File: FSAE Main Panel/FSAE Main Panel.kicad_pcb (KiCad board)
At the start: 2 copper layers, 1 part

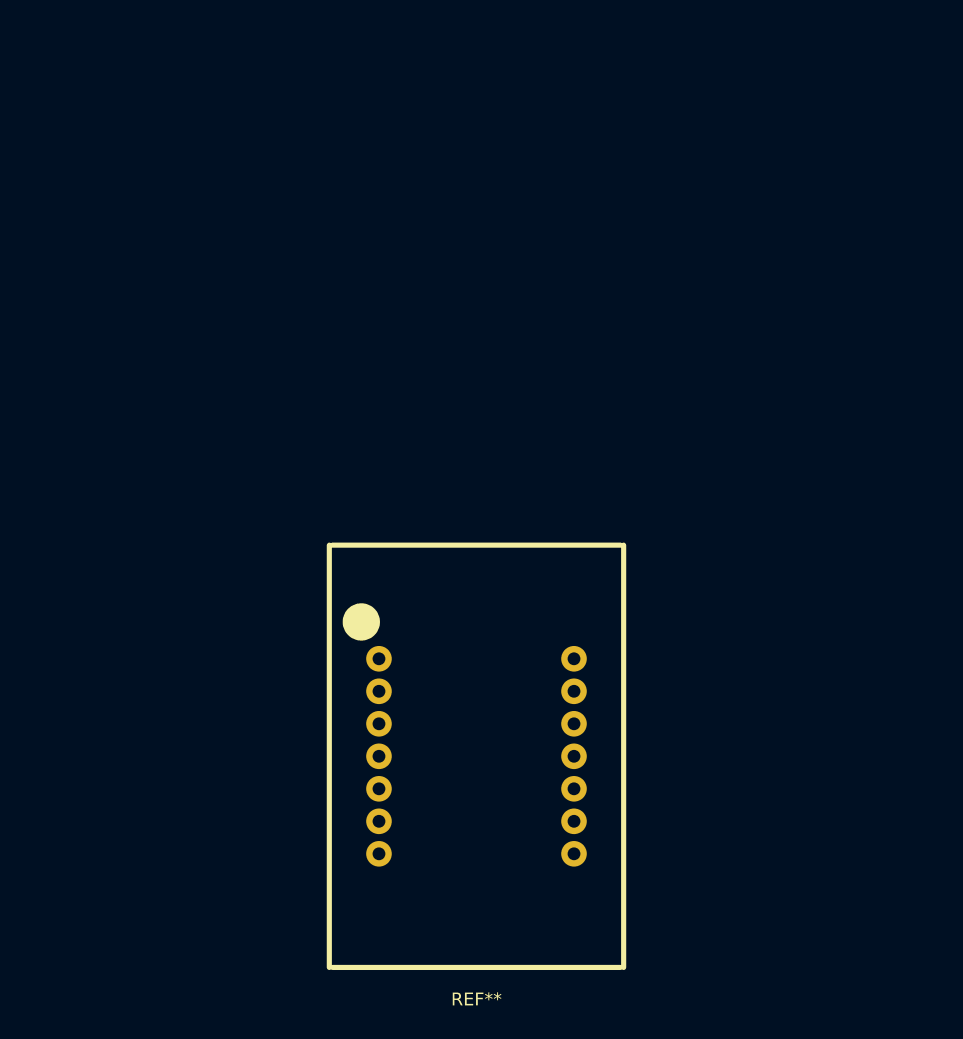
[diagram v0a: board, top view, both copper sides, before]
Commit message: Initial PCB layout
Started PCB layout with major dimensions.
Added RPM LEDs.
Rearranged the file structure for the librarys and the search paths.
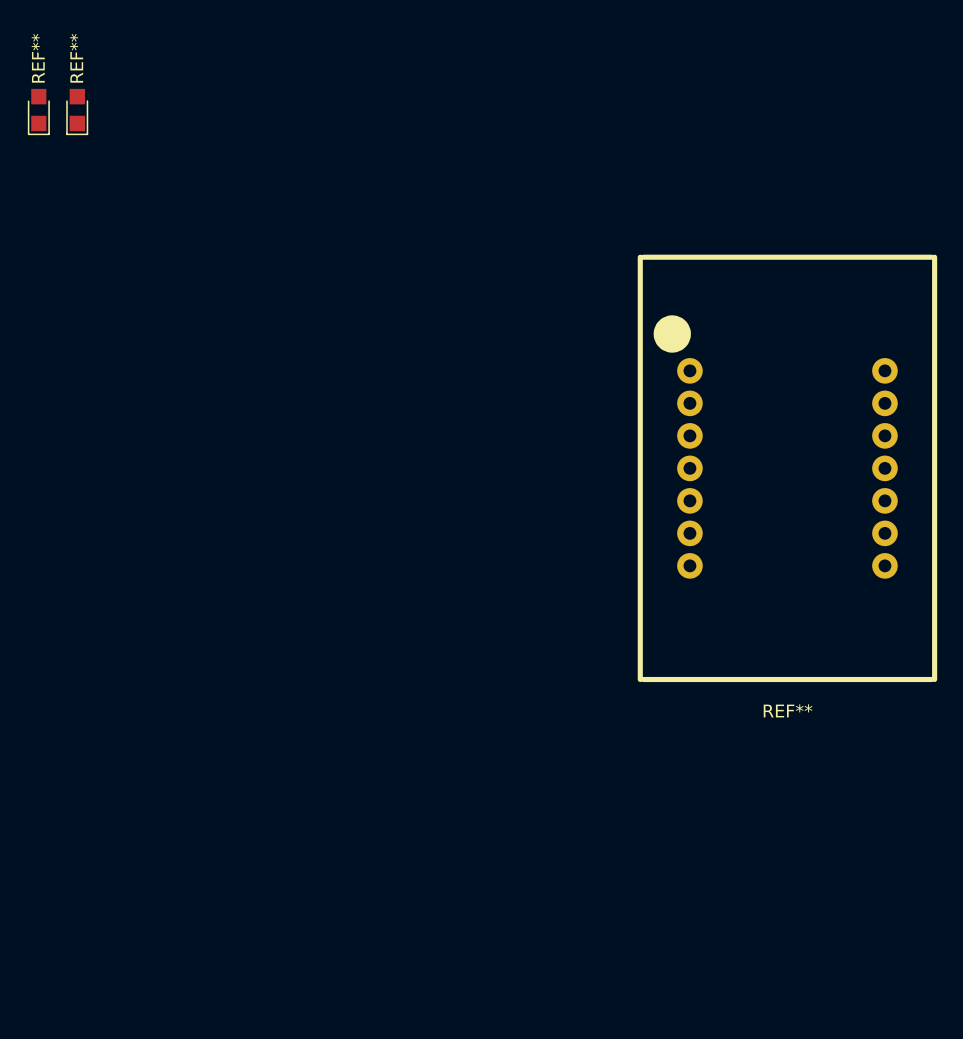
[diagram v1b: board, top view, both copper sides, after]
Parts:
- added REF**: LED_0805, OSRAM:D_0805, F.Cu at (104.0, 37.5)
- added REF**: LED_0805, OSRAM:D_0805, F.Cu at (107.0, 37.5)
- moved REF** 33.1 mm to (162.5, 65.5)
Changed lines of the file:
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@@
     (links 0)
     (no_connects 0)
-    (area 0 0 0 0)
+    (area 124.924999 69.724999 151.475001 108.075)
     (thickness 1.6)
-    (drawings 0)
+    (drawings 13)
     (tracks 0)
     (zones 0)
-    (modules 1)
+    (modules 3)
     (nets 1)
   )
@@
     (pad_to_mask_clearance 0.2)
     (aux_axis_origin 0 0)
-    (visible_elements FFFFFF7F)
+    (visible_elements 7FFFFFFF)
     (pcbplotparams
       (layerselection 0x00030_80000001)
@@
   )
   (module Kingbright:SC10-11EWA (layer F.Cu)
-    (at 138.2 88)
+    (at 162.5 65.5)
     (tags "26mm 7 segment")
     (fp_text reference REF** (at 0 19) (layer F.SilkS)
@@
     (pad 1 thru_hole circle (at -7.62 -7.62) (size 2 2) (drill 1) (layers *.Cu *.Mask))
   )
+  (module OSRAM:D_0805 (layer F.Cu)
+    (at 104 37.5 90)
+    (descr "Diode SMD in 0805 package http://datasheets.avx.com/schottky.pdf")
+    (tags "smd diode")
+    (attr smd)
+    (fp_text reference REF** (at 4 0 90) (layer F.SilkS)
+      (effects (font (size 1 1) (thickness 0.15)))
+    )
+    (fp_text value LED_0805 (at -6 0 90) (layer F.Fab)
+      (effects (font (size 1 1) (thickness 0.15)))
+    )
+    (fp_line (start -0.1 -0.4) (end -0.1 0.4) (layer F.Fab) (width 0.05))
+    (fp_text user %R (at 4 0 90) (layer F.Fab)
+      (effects (font (size 1 1) (thickness 0.15)))
+    )
+    (fp_line (start -1.9 -0.8) (end -1.9 0.8) (layer F.SilkS) (width 0.12))
+    (fp_line (start -2 0.88) (end -2 -0.88) (layer F.CrtYd) (width 0.05))
+    (fp_line (start 1.7 0.88) (end -2 0.88) (layer F.CrtYd) (width 0.05))
+    (fp_line (start 1.7 -0.88) (end 1.7 0.88) (layer F.CrtYd) (width 0.05))
+    (fp_line (start -2 -0.88) (end 1.7 -0.88) (layer F.CrtYd) (width 0.05))
+    (fp_line (start 0.2 0) (end 0.4 0) (layer F.Fab) (width 0.1))
+    (fp_line (start 0.2 0.2) (end 0.2 -0.2) (layer F.Fab) (width 0.1))
+    (fp_line (start -0.1 0) (end 0.2 0.2) (layer F.Fab) (width 0.1))
+    (fp_line (start 0.2 -0.2) (end -0.1 0) (layer F.Fab) (width 0.1))
+    (fp_line (start -1 0.65) (end -1 -0.65) (layer F.Fab) (width 0.1))
+    (fp_line (start 1 0.65) (end -1 0.65) (layer F.Fab) (width 0.1))
+    (fp_line (start 1 -0.65) (end 1 0.65) (layer F.Fab) (width 0.1))
+    (fp_line (start -1 -0.65) (end 1 -0.65) (layer F.Fab) (width 0.1))
+    (fp_line (start -1.9 0.8) (end 0.7 0.8) (layer F.SilkS) (width 0.12))
+    (fp_line (start -1.9 -0.8) (end 0.7 -0.8) (layer F.SilkS) (width 0.12))
+    (pad 1 smd rect (at -1.05 0 90) (size 1.2 1.2) (layers F.Cu F.Paste F.Mask))
+    (pad 2 smd rect (at 1.05 0 90) (size 1.2 1.2) (layers F.Cu F.Paste F.Mask))
+    (model ${KISYS3DMOD}/Diodes_SMD.3dshapes/D_0805.wrl
+      (at (xyz 0 0 0))
+      (scale (xyz 1 1 1))
+      (rotate (xyz 0 0 0))
+    )
+  )
+  (module OSRAM:D_0805 (layer F.Cu)
+    (at 107 37.5 90)
+    (descr "Diode SMD in 0805 package http://datasheets.avx.com/schottky.pdf")
+    (tags "smd diode")
+    (attr smd)
+    (fp_text reference REF** (at 4 0 90) (layer F.SilkS)
+      (effects (font (size 1 1) (thickness 0.15)))
+    )
+    (fp_text value LED_0805 (at -6 0 90) (layer F.Fab)
+      (effects (font (size 1 1) (thickness 0.15)))
+    )
+    (fp_line (start -0.1 -0.4) (end -0.1 0.4) (layer F.Fab) (width 0.05))
+    (fp_text user %R (at 4 0 90) (layer F.Fab)
+      (effects (font (size 1 1) (thickness 0.15)))
+    )
+    (fp_line (start -1.9 -0.8) (end -1.9 0.8) (layer F.SilkS) (width 0.12))
+    (fp_line (start -2 0.88) (end -2 -0.88) (layer F.CrtYd) (width 0.05))
+    (fp_line (start 1.7 0.88) (end -2 0.88) (layer F.CrtYd) (width 0.05))
+    (fp_line (start 1.7 -0.88) (end 1.7 0.88) (layer F.CrtYd) (width 0.05))
+    (fp_line (start -2 -0.88) (end 1.7 -0.88) (layer F.CrtYd) (width 0.05))
+    (fp_line (start 0.2 0) (end 0.4 0) (layer F.Fab) (width 0.1))
+    (fp_line (start 0.2 0.2) (end 0.2 -0.2) (layer F.Fab) (width 0.1))
+    (fp_line (start -0.1 0) (end 0.2 0.2) (layer F.Fab) (width 0.1))
+    (fp_line (start 0.2 -0.2) (end -0.1 0) (layer F.Fab) (width 0.1))
+    (fp_line (start -1 0.65) (end -1 -0.65) (layer F.Fab) (width 0.1))
+    (fp_line (start 1 0.65) (end -1 0.65) (layer F.Fab) (width 0.1))
+    (fp_line (start 1 -0.65) (end 1 0.65) (layer F.Fab) (width 0.1))
+    (fp_line (start -1 -0.65) (end 1 -0.65) (layer F.Fab) (width 0.1))
+    (fp_line (start -1.9 0.8) (end 0.7 0.8) (layer F.SilkS) (width 0.12))
+    (fp_line (start -1.9 -0.8) (end 0.7 -0.8) (layer F.SilkS) (width 0.12))
+    (pad 1 smd rect (at -1.05 0 90) (size 1.2 1.2) (layers F.Cu F.Paste F.Mask))
+    (pad 2 smd rect (at 1.05 0 90) (size 1.2 1.2) (layers F.Cu F.Paste F.Mask))
+    (model ${KISYS3DMOD}/Diodes_SMD.3dshapes/D_0805.wrl
+      (at (xyz 0 0 0))
+      (scale (xyz 1 1 1))
+      (rotate (xyz 0 0 0))
+    )
+  )
+  (dimension 8 (width 0.3) (layer Margin)
+    (gr_text 8mm (at 177.85 45 270) (layer Margin)
+      (effects (font (size 1.5 1.5) (thickness 0.3)))
+    )
+    (feature1 (pts (xy 174 49) (xy 179.2 49)))
+    (feature2 (pts (xy 174 41) (xy 179.2 41)))
+    (crossbar (pts (xy 176.5 41) (xy 176.5 49)))
+    (arrow1a (pts (xy 176.5 49) (xy 175.913579 47.873496)))
+    (arrow1b (pts (xy 176.5 49) (xy 177.086421 47.873496)))
+    (arrow2a (pts (xy 176.5 41) (xy 175.913579 42.126504)))
+    (arrow2b (pts (xy 176.5 41) (xy 177.086421 42.126504)))
+  )
+  (dimension 33 (width 0.3) (layer Margin)
+    (gr_text 33mm (at 177.85 65.5 270) (layer Margin)
+      (effects (font (size 1.5 1.5) (thickness 0.3)))
+    )
+    (feature1 (pts (xy 174 82) (xy 179.2 82)))
+    (feature2 (pts (xy 174 49) (xy 179.2 49)))
+    (crossbar (pts (xy 176.5 49) (xy 176.5 82)))
+    (arrow1a (pts (xy 176.5 82) (xy 175.913579 80.873496)))
+    (arrow1b (pts (xy 176.5 82) (xy 177.086421 80.873496)))
+    (arrow2a (pts (xy 176.5 49) (xy 175.913579 50.126504)))
+    (arrow2b (pts (xy 176.5 49) (xy 177.086421 50.126504)))
+  )
+  (dimension 23 (width 0.3) (layer Margin)
+    (gr_text 23mm (at 162.5 85.349999) (layer Margin)
+      (effects (font (size 1.5 1.5) (thickness 0.3)))
+    )
+    (feature1 (pts (xy 174 82) (xy 174 86.699999)))
+    (feature2 (pts (xy 151 82) (xy 151 86.699999)))
+    (crossbar (pts (xy 151 83.999999) (xy 174 83.999999)))
+    (arrow1a (pts (xy 174 83.999999) (xy 172.873496 84.58642)))
+    (arrow1b (pts (xy 174 83.999999) (xy 172.873496 83.413578)))
+    (arrow2a (pts (xy 151 83.999999) (xy 152.126504 84.58642)))
+    (arrow2b (pts (xy 151 83.999999) (xy 152.126504 83.413578)))
+  )
+  (gr_line (start 151 82) (end 174 82) (angle 90) (layer Margin) (width 0.2))
+  (gr_line (start 151 49) (end 151 82) (angle 90) (layer Margin) (width 0.2))
+  (gr_line (start 174 49) (end 174 82) (angle 90) (layer Margin) (width 0.2))
+  (gr_line (start 151 49) (end 174 49) (angle 90) (layer Margin) (width 0.2))
+  (dimension 125 (width 0.3) (layer Margin)
+    (gr_text 125mm (at 165 31.15) (layer Margin)
+      (effects (font (size 1.5 1.5) (thickness 0.3)))
+    )
+    (feature1 (pts (xy 227.5 35) (xy 227.5 29.8)))
+    (feature2 (pts (xy 102.5 35) (xy 102.5 29.8)))
+    (crossbar (pts (xy 102.5 32.5) (xy 227.5 32.5)))
+    (arrow1a (pts (xy 227.5 32.5) (xy 226.373496 33.086421)))
+    (arrow1b (pts (xy 227.5 32.5) (xy 226.373496 31.913579)))
+    (arrow2a (pts (xy 102.5 32.5) (xy 103.626504 33.086421)))
+    (arrow2b (pts (xy 102.5 32.5) (xy 103.626504 31.913579)))
+  )
+  (dimension 6 (width 0.3) (layer Margin)
+    (gr_text 6mm (at 238 38 90) (layer Margin)
+      (effects (font (size 1.5 1.5) (thickness 0.3)))
+    )
+    (feature1 (pts (xy 227.5 35) (xy 236.7 35)))
+    (feature2 (pts (xy 227.5 41) (xy 236.7 41)))
+    (crossbar (pts (xy 234 41) (xy 234 35)))
+    (arrow1a (pts (xy 234 35) (xy 234.586421 36.126504)))
+    (arrow1b (pts (xy 234 35) (xy 233.413579 36.126504)))
+    (arrow2a (pts (xy 234 41) (xy 234.586421 39.873496)))
+    (arrow2b (pts (xy 234 41) (xy 233.413579 39.873496)))
+  )
+  (gr_line (start 102.5 35) (end 102.5 41) (angle 90) (layer Margin) (width 0.2))
+  (gr_line (start 227.5 35) (end 227.5 41) (angle 90) (layer Margin) (width 0.2))
+  (gr_line (start 102.5 41) (end 227.5 41) (angle 90) (layer Margin) (width 0.2))
+  (gr_line (start 227.5 35) (end 102.5 35) (angle 90) (layer Margin) (width 0.2))
 )

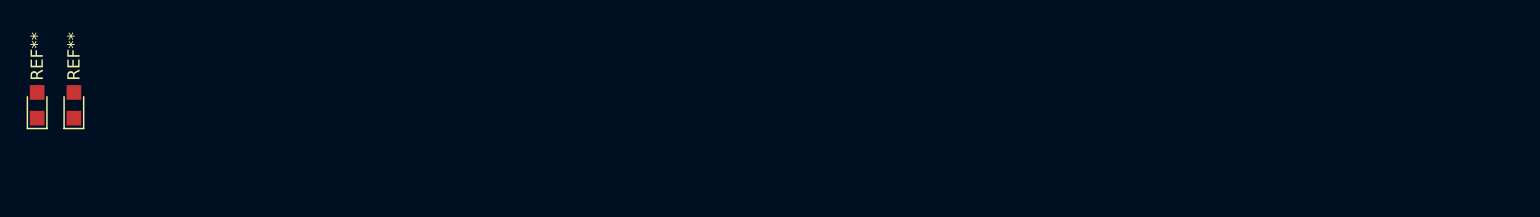
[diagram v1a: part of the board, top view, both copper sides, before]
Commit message: Added RPM LED Control
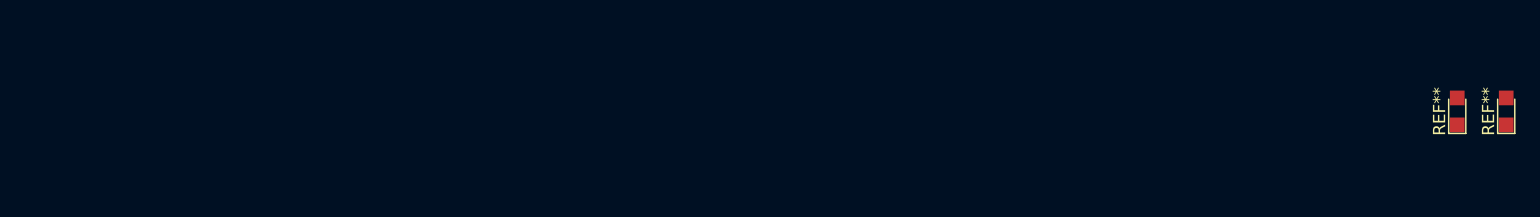
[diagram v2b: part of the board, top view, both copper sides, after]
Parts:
- removed the REF** at (104.0, 37.5)
- removed the REF** at (107.0, 37.5)
- added REF**: LED_0805, LEDs:LED_0805, F.Cu at (224.0, 38.0)
- added REF**: LED_0805, LEDs:LED_0805, F.Cu at (220.0, 38.0)
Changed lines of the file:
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@@
     (links 0)
     (no_connects 0)
-    (area 124.924999 69.724999 151.475001 108.075)
+    (area 102.399999 29.8 240.714287 86.7)
     (thickness 1.6)
     (drawings 13)
@@
     (pad 1 thru_hole circle (at -7.62 -7.62) (size 2 2) (drill 1) (layers *.Cu *.Mask))
   )
-  (module OSRAM:D_0805 (layer F.Cu)
-    (at 104 37.5 90)
-    (descr "Diode SMD in 0805 package http://datasheets.avx.com/schottky.pdf")
-    (tags "smd diode")
+  (module LEDs:LED_0805 (layer F.Cu)
+    (at 224 38 90)
+    (descr "LED 0805 smd package")
+    (tags "LED led 0805 SMD smd SMT smt smdled SMDLED smtled SMTLED")
     (attr smd)
-    (fp_text reference REF** (at 4 0 90) (layer F.SilkS)
-      (effects (font (size 1 1) (thickness 0.15)))
-    )
-    (fp_text value LED_0805 (at -6 0 90) (layer F.Fab)
-      (effects (font (size 1 1) (thickness 0.15)))
-    )
-    (fp_line (start -0.1 -0.4) (end -0.1 0.4) (layer F.Fab) (width 0.05))
-    (fp_text user %R (at 4 0 90) (layer F.Fab)
-      (effects (font (size 1 1) (thickness 0.15)))
-    )
-    (fp_line (start -1.9 -0.8) (end -1.9 0.8) (layer F.SilkS) (width 0.12))
-    (fp_line (start -2 0.88) (end -2 -0.88) (layer F.CrtYd) (width 0.05))
-    (fp_line (start 1.7 0.88) (end -2 0.88) (layer F.CrtYd) (width 0.05))
-    (fp_line (start 1.7 -0.88) (end 1.7 0.88) (layer F.CrtYd) (width 0.05))
-    (fp_line (start -2 -0.88) (end 1.7 -0.88) (layer F.CrtYd) (width 0.05))
-    (fp_line (start 0.2 0) (end 0.4 0) (layer F.Fab) (width 0.1))
-    (fp_line (start 0.2 0.2) (end 0.2 -0.2) (layer F.Fab) (width 0.1))
-    (fp_line (start -0.1 0) (end 0.2 0.2) (layer F.Fab) (width 0.1))
-    (fp_line (start 0.2 -0.2) (end -0.1 0) (layer F.Fab) (width 0.1))
-    (fp_line (start -1 0.65) (end -1 -0.65) (layer F.Fab) (width 0.1))
-    (fp_line (start 1 0.65) (end -1 0.65) (layer F.Fab) (width 0.1))
-    (fp_line (start 1 -0.65) (end 1 0.65) (layer F.Fab) (width 0.1))
-    (fp_line (start -1 -0.65) (end 1 -0.65) (layer F.Fab) (width 0.1))
-    (fp_line (start -1.9 0.8) (end 0.7 0.8) (layer F.SilkS) (width 0.12))
-    (fp_line (start -1.9 -0.8) (end 0.7 -0.8) (layer F.SilkS) (width 0.12))
-    (pad 1 smd rect (at -1.05 0 90) (size 1.2 1.2) (layers F.Cu F.Paste F.Mask))
-    (pad 2 smd rect (at 1.05 0 90) (size 1.2 1.2) (layers F.Cu F.Paste F.Mask))
-    (model ${KISYS3DMOD}/Diodes_SMD.3dshapes/D_0805.wrl
+    (fp_text reference REF** (at 0 -1.45 90) (layer F.SilkS)
+      (effects (font (size 1 1) (thickness 0.15)))
+    )
+    (fp_text value LED_0805 (at 0 1.55 90) (layer F.Fab)
+      (effects (font (size 1 1) (thickness 0.15)))
+    )
+    (fp_line (start -1.8 -0.7) (end -1.8 0.7) (layer F.SilkS) (width 0.12))
+    (fp_line (start -0.4 -0.4) (end -0.4 0.4) (layer F.Fab) (width 0.1))
+    (fp_line (start -0.4 0) (end 0.2 -0.4) (layer F.Fab) (width 0.1))
+    (fp_line (start 0.2 0.4) (end -0.4 0) (layer F.Fab) (width 0.1))
+    (fp_line (start 0.2 -0.4) (end 0.2 0.4) (layer F.Fab) (width 0.1))
+    (fp_line (start 1 0.6) (end -1 0.6) (layer F.Fab) (width 0.1))
+    (fp_line (start 1 -0.6) (end 1 0.6) (layer F.Fab) (width 0.1))
+    (fp_line (start -1 -0.6) (end 1 -0.6) (layer F.Fab) (width 0.1))
+    (fp_line (start -1 0.6) (end -1 -0.6) (layer F.Fab) (width 0.1))
+    (fp_line (start -1.8 0.7) (end 1 0.7) (layer F.SilkS) (width 0.12))
+    (fp_line (start -1.8 -0.7) (end 1 -0.7) (layer F.SilkS) (width 0.12))
+    (fp_line (start 1.95 -0.85) (end 1.95 0.85) (layer F.CrtYd) (width 0.05))
+    (fp_line (start 1.95 0.85) (end -1.95 0.85) (layer F.CrtYd) (width 0.05))
+    (fp_line (start -1.95 0.85) (end -1.95 -0.85) (layer F.CrtYd) (width 0.05))
+    (fp_line (start -1.95 -0.85) (end 1.95 -0.85) (layer F.CrtYd) (width 0.05))
+    (fp_text user %R (at 0 -1.25 90) (layer F.Fab)
+      (effects (font (size 0.4 0.4) (thickness 0.1)))
+    )
+    (pad 2 smd rect (at 1.1 0 270) (size 1.2 1.2) (layers F.Cu F.Paste F.Mask))
+    (pad 1 smd rect (at -1.1 0 270) (size 1.2 1.2) (layers F.Cu F.Paste F.Mask))
+    (model ${KISYS3DMOD}/LEDs.3dshapes/LED_0805.wrl
       (at (xyz 0 0 0))
       (scale (xyz 1 1 1))
-      (rotate (xyz 0 0 0))
-    )
-  )
-  (module OSRAM:D_0805 (layer F.Cu)
-    (at 107 37.5 90)
-    (descr "Diode SMD in 0805 package http://datasheets.avx.com/schottky.pdf")
-    (tags "smd diode")
+      (rotate (xyz 0 0 180))
+    )
+  )
+  (module LEDs:LED_0805 (layer F.Cu)
+    (at 220 38 90)
+    (descr "LED 0805 smd package")
+    (tags "LED led 0805 SMD smd SMT smt smdled SMDLED smtled SMTLED")
     (attr smd)
-    (fp_text reference REF** (at 4 0 90) (layer F.SilkS)
-      (effects (font (size 1 1) (thickness 0.15)))
-    )
-    (fp_text value LED_0805 (at -6 0 90) (layer F.Fab)
-      (effects (font (size 1 1) (thickness 0.15)))
-    )
-    (fp_line (start -0.1 -0.4) (end -0.1 0.4) (layer F.Fab) (width 0.05))
-    (fp_text user %R (at 4 0 90) (layer F.Fab)
-      (effects (font (size 1 1) (thickness 0.15)))
-    )
-    (fp_line (start -1.9 -0.8) (end -1.9 0.8) (layer F.SilkS) (width 0.12))
-    (fp_line (start -2 0.88) (end -2 -0.88) (layer F.CrtYd) (width 0.05))
-    (fp_line (start 1.7 0.88) (end -2 0.88) (layer F.CrtYd) (width 0.05))
-    (fp_line (start 1.7 -0.88) (end 1.7 0.88) (layer F.CrtYd) (width 0.05))
-    (fp_line (start -2 -0.88) (end 1.7 -0.88) (layer F.CrtYd) (width 0.05))
-    (fp_line (start 0.2 0) (end 0.4 0) (layer F.Fab) (width 0.1))
-    (fp_line (start 0.2 0.2) (end 0.2 -0.2) (layer F.Fab) (width 0.1))
-    (fp_line (start -0.1 0) (end 0.2 0.2) (layer F.Fab) (width 0.1))
-    (fp_line (start 0.2 -0.2) (end -0.1 0) (layer F.Fab) (width 0.1))
-    (fp_line (start -1 0.65) (end -1 -0.65) (layer F.Fab) (width 0.1))
-    (fp_line (start 1 0.65) (end -1 0.65) (layer F.Fab) (width 0.1))
-    (fp_line (start 1 -0.65) (end 1 0.65) (layer F.Fab) (width 0.1))
-    (fp_line (start -1 -0.65) (end 1 -0.65) (layer F.Fab) (width 0.1))
-    (fp_line (start -1.9 0.8) (end 0.7 0.8) (layer F.SilkS) (width 0.12))
-    (fp_line (start -1.9 -0.8) (end 0.7 -0.8) (layer F.SilkS) (width 0.12))
-    (pad 1 smd rect (at -1.05 0 90) (size 1.2 1.2) (layers F.Cu F.Paste F.Mask))
-    (pad 2 smd rect (at 1.05 0 90) (size 1.2 1.2) (layers F.Cu F.Paste F.Mask))
-    (model ${KISYS3DMOD}/Diodes_SMD.3dshapes/D_0805.wrl
+    (fp_text reference REF** (at 0 -1.45 90) (layer F.SilkS)
+      (effects (font (size 1 1) (thickness 0.15)))
+    )
+    (fp_text value LED_0805 (at 0 1.55 90) (layer F.Fab)
+      (effects (font (size 1 1) (thickness 0.15)))
+    )
+    (fp_line (start -1.8 -0.7) (end -1.8 0.7) (layer F.SilkS) (width 0.12))
+    (fp_line (start -0.4 -0.4) (end -0.4 0.4) (layer F.Fab) (width 0.1))
+    (fp_line (start -0.4 0) (end 0.2 -0.4) (layer F.Fab) (width 0.1))
+    (fp_line (start 0.2 0.4) (end -0.4 0) (layer F.Fab) (width 0.1))
+    (fp_line (start 0.2 -0.4) (end 0.2 0.4) (layer F.Fab) (width 0.1))
+    (fp_line (start 1 0.6) (end -1 0.6) (layer F.Fab) (width 0.1))
+    (fp_line (start 1 -0.6) (end 1 0.6) (layer F.Fab) (width 0.1))
+    (fp_line (start -1 -0.6) (end 1 -0.6) (layer F.Fab) (width 0.1))
+    (fp_line (start -1 0.6) (end -1 -0.6) (layer F.Fab) (width 0.1))
+    (fp_line (start -1.8 0.7) (end 1 0.7) (layer F.SilkS) (width 0.12))
+    (fp_line (start -1.8 -0.7) (end 1 -0.7) (layer F.SilkS) (width 0.12))
+    (fp_line (start 1.95 -0.85) (end 1.95 0.85) (layer F.CrtYd) (width 0.05))
+    (fp_line (start 1.95 0.85) (end -1.95 0.85) (layer F.CrtYd) (width 0.05))
+    (fp_line (start -1.95 0.85) (end -1.95 -0.85) (layer F.CrtYd) (width 0.05))
+    (fp_line (start -1.95 -0.85) (end 1.95 -0.85) (layer F.CrtYd) (width 0.05))
+    (fp_text user %R (at 0 -1.25 90) (layer F.Fab)
+      (effects (font (size 0.4 0.4) (thickness 0.1)))
+    )
+    (pad 2 smd rect (at 1.1 0 270) (size 1.2 1.2) (layers F.Cu F.Paste F.Mask))
+    (pad 1 smd rect (at -1.1 0 270) (size 1.2 1.2) (layers F.Cu F.Paste F.Mask))
+    (model ${KISYS3DMOD}/LEDs.3dshapes/LED_0805.wrl
       (at (xyz 0 0 0))
       (scale (xyz 1 1 1))
-      (rotate (xyz 0 0 0))
-    )
-  )
+      (rotate (xyz 0 0 180))
+    )
+  )
